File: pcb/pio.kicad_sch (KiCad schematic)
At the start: 32 parts, among them J11 BM04B-SRSS-TB, J4 BM06B-SRSS-TB, J5 BM06B-SRSS-TB, J6 BM04B-SRSS-TB, J7 BM06B-SRSS-TB, U4 MCP23017T-E/ML

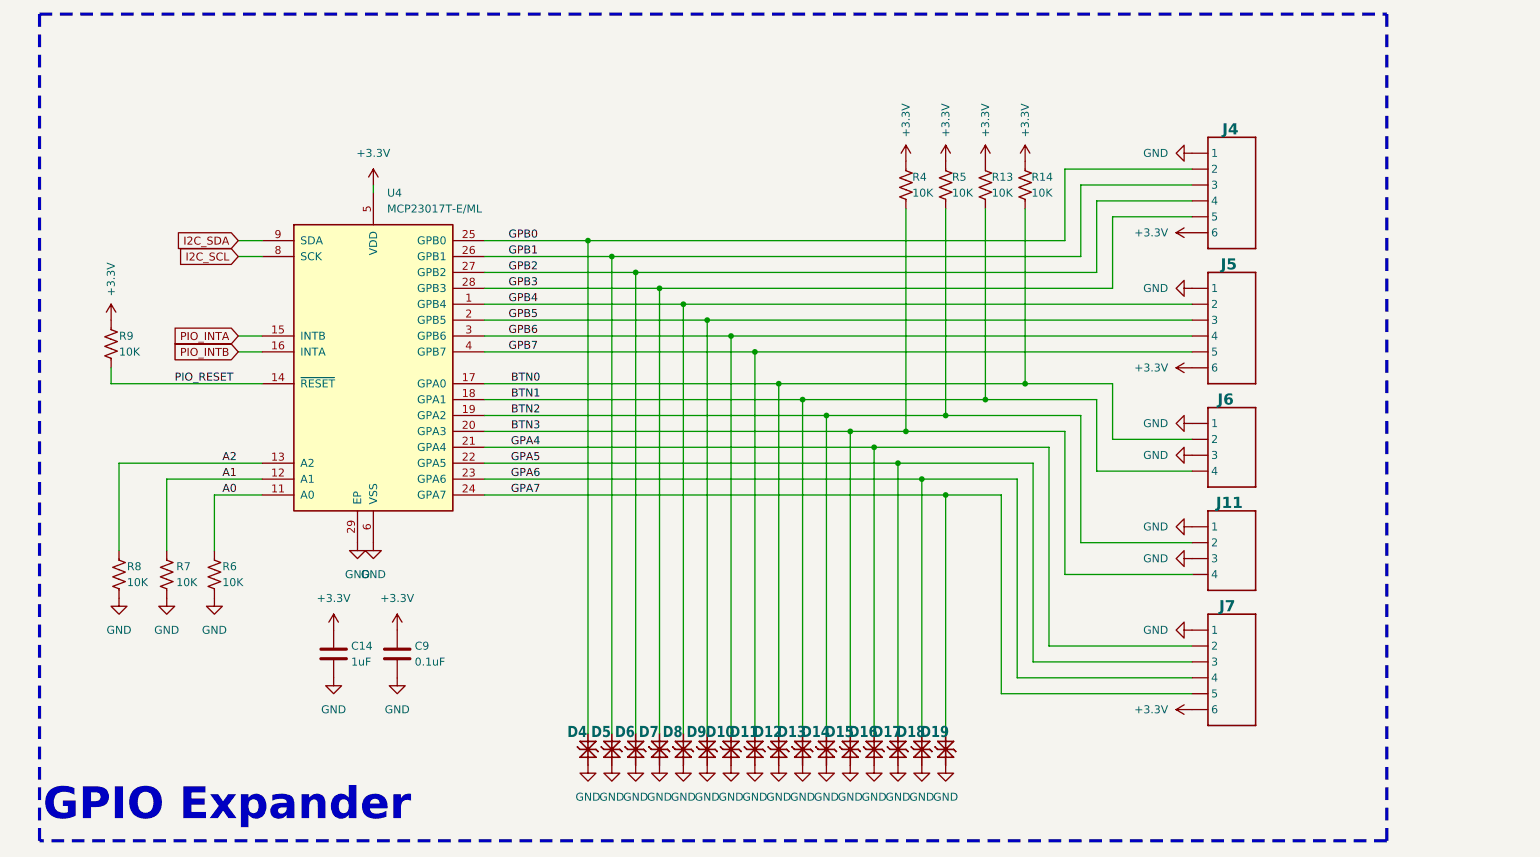
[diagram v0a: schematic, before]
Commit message: Updated license and minor schematic changes
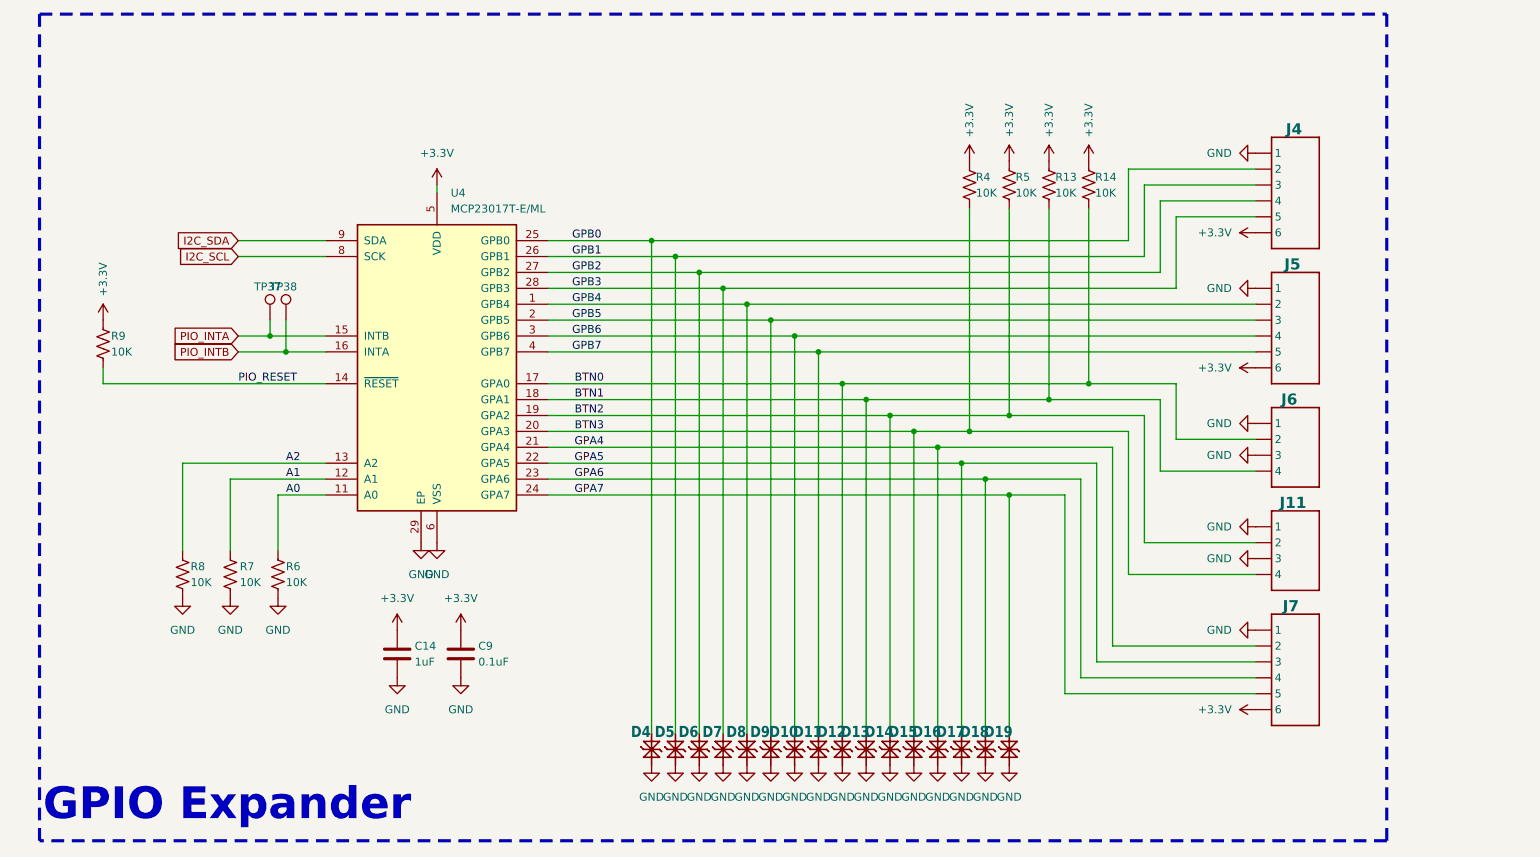
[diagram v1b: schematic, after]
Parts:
- added TP37, TP38: TP, CRGM Mechanical:TestPoint_Pad_D1.0mm, symbol Connector:TestPoint
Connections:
- net PIO_INTA: now also TP37.1
- net PIO_INTB: now also TP38.1
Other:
- moved on the sheet: C14, C9, D10, D11, D12, D13, D14, D15, D16, D17, D18, D19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

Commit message: Change name in schematic
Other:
- title: Node Hardware -> Hub Hardware
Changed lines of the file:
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@@
 	(paper "A4")
 	(title_block
-		(title "Node Hardware")
+		(title "Hub Hardware")
 		(date "<<release-date>>")
 		(rev "<<tag>>")

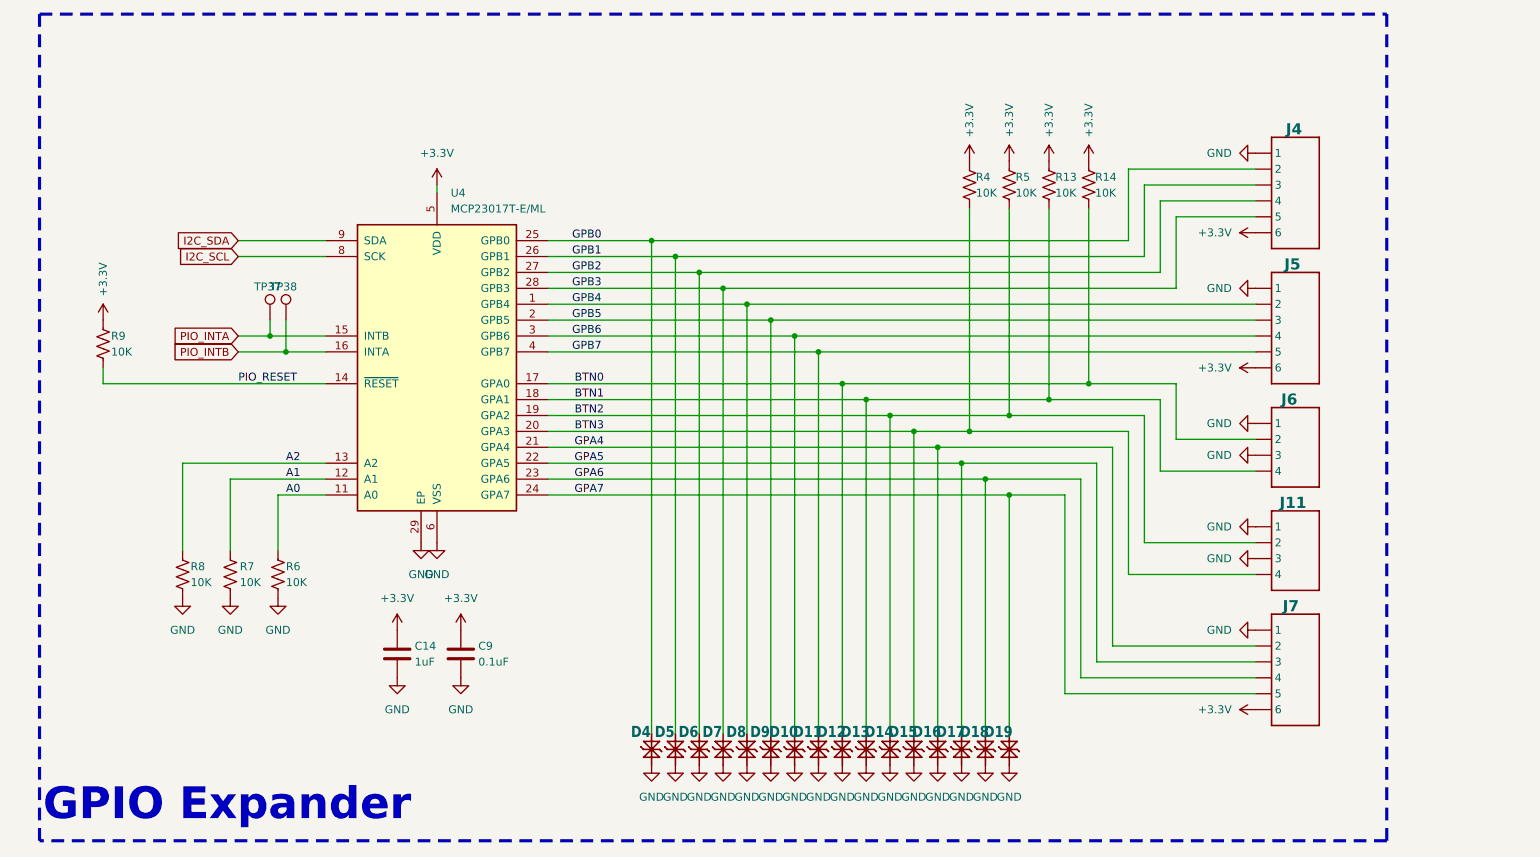
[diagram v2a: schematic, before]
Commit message: Renamed peripherals to interfaces; added test points; added led jumper
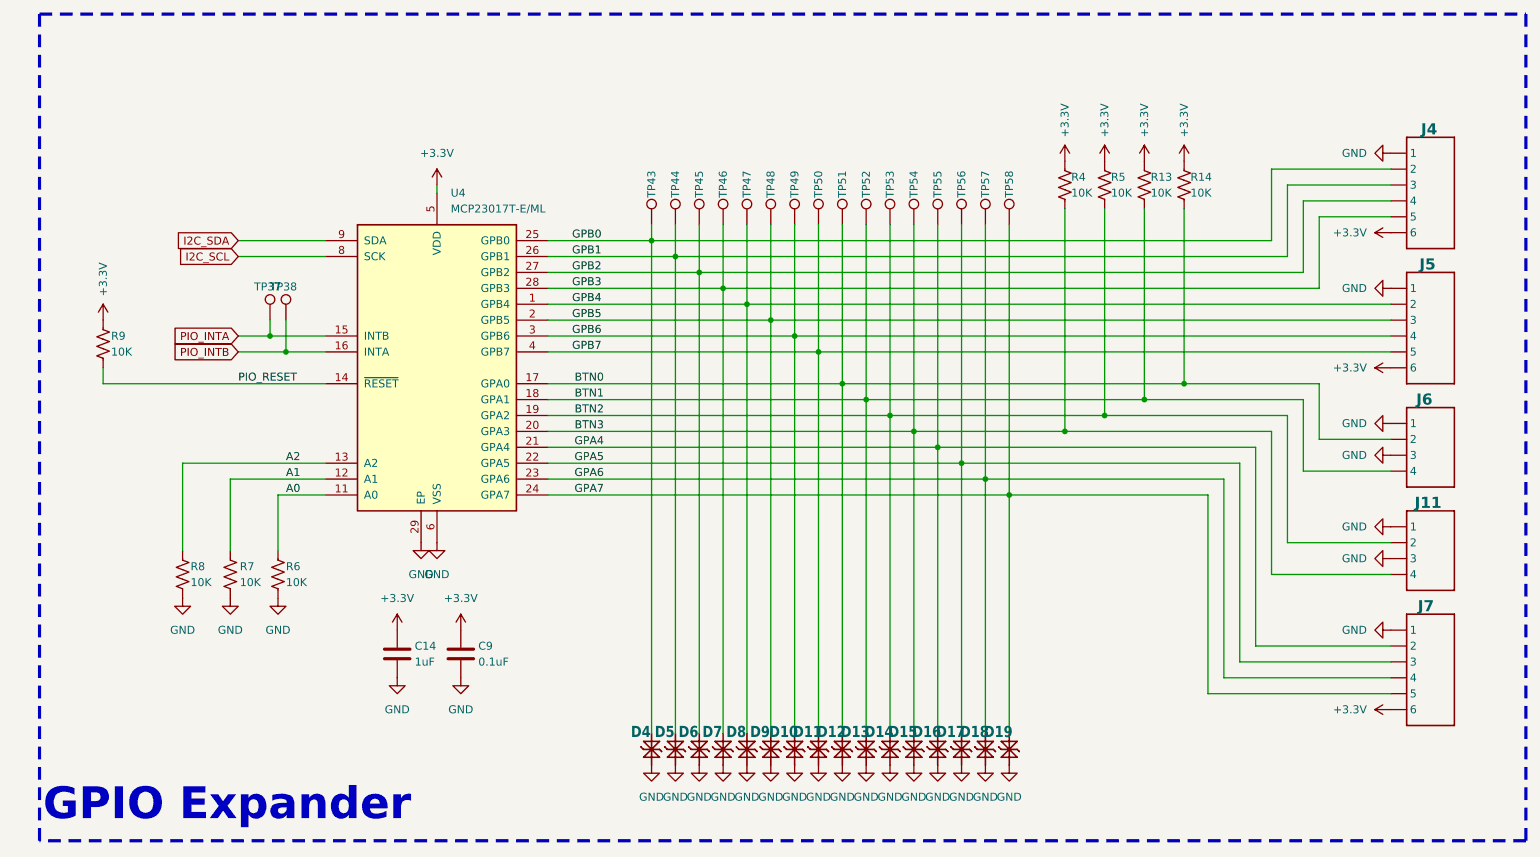
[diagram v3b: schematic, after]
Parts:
- added TP43, TP44, TP45, TP46, TP47, TP48, TP49, TP50, TP51, TP52, TP53, TP54, TP55, TP56, TP57, TP58: ~, CRGM Mechanical:TestPoint_Pad_D1.0mm, symbol Connector:TestPoint
- TP37, TP38: value TP -> ~
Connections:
- net BTN0: now also TP51.1
- net BTN1: now also TP52.1
- net BTN2: now also TP53.1
- net BTN3: now also TP54.1
- net GPA4: now also TP55.1
- net GPA5: now also TP56.1
- net GPA6: now also TP57.1
- net GPA7: now also TP58.1
- net GPB0: now also TP43.1
- net GPB1: now also TP44.1
- net GPB2: now also TP45.1
- net GPB3: now also TP46.1
- net GPB4: now also TP47.1
- net GPB5: now also TP48.1
- net GPB6: now also TP49.1
- net GPB7: now also TP50.1
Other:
- moved on the sheet: J11, J4, J5, J6, J7, R13, R14, R4, R5

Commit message: Adjusting for consistency
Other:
- title: Hub Hardware -> Aquarius Hub
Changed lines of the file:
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@@
 	(paper "A4")
 	(title_block
-		(title "Hub Hardware")
+		(title "Aquarius Hub")
 		(date "<<release-date>>")
 		(rev "<<tag>>")

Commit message: Sync symbols and footprints
Transitioned to CRGM footprints
Added dimensions
Fixed some spacing
Adjusted properties
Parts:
- C14, C9: footprint Capacitor_SMD:C_0603_1608Metric -> CRGM Passive:C_0603_1608Metric
- J11, J6: LCSC C2919601 -> C2763614
- J4, J5, J7: MPN BM06B-SRSS-TB -> BM06B-SRSS-TBT(LF)(SN)
- R13, R14, R4, R5, R6, R7, R8, R9: footprint Resistor_SMD:R_0603_1608Metric -> CRGM Passive:R_0603_1608Metric
- U4: footprint Package_DFN_QFN:QFN-28-1EP_6x6mm_P0.65mm_EP4.25x4.25mm -> CRG Makes:QFN-28-1EP_6x6mm_P0.65mm_EP4.25x4.25mm
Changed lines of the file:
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@@
 			)
 		)
-		(property "Footprint" "Resistor_SMD:R_0603_1608Metric"
+		(property "Footprint" "CRGM Passive:R_0603_1608Metric"
 			(at 200.406 43.434 90)
 			(effects
@@
 			)
 		)
-		(property "Footprint" "Resistor_SMD:R_0603_1608Metric"
+		(property "Footprint" "CRGM Passive:R_0603_1608Metric"
 			(at 48.006 105.664 90)
 			(effects
@@
 			)
 		)
-		(property "Footprint" "Package_DFN_QFN:QFN-28-1EP_6x6mm_P0.65mm_EP4.25x4.25mm"
+		(property "Footprint" "CRG Makes:QFN-28-1EP_6x6mm_P0.65mm_EP4.25x4.25mm"
 			(at 85.09 97.79 0)
 			(effects
@@
 			)
 		)
-		(property "Description" "JST SH 1.0mm 4 Position Vertical"
+		(property "Description" "4 Position, 1mm pitch"
 			(at 237.998 89.408 0)
 			(effects
@@
 			)
 		)
-		(property "LCSC" "C2919601"
+		(property "LCSC" "C2763614"
 			(at 237.998 80.01 0)
 			(effects
@@
 			)
 		)
-		(property "Footprint" "Capacitor_SMD:C_0603_1608Metric"
+		(property "Footprint" "CRGM Passive:C_0603_1608Metric"
 			(at 74.6252 121.92 0)
 			(effects
@@
 			)
 		)
-		(property "Footprint" "Resistor_SMD:R_0603_1608Metric"
+		(property "Footprint" "CRGM Passive:R_0603_1608Metric"
 			(at 187.706 43.434 90)
 			(effects
@@
 		)
 		(property "Footprint" "CRGM Connector:JST_SH_BM06B-SRSS-TB_1x06-1MP_P1.00mm_Vertical"
-			(at 234.95 114.3 0)
+			(at 236.474 104.648 0)
 			(effects
 				(font
@@
 			)
 		)
-		(property "Datasheet" "https://www.digikey.com/en/products/detail/jst-sales-america-inc/BM06B-SRSS-TB/926698"
-			(at 234.95 114.3 0)
+		(property "Datasheet" "https://www.jst-mfg.com/product/pdf/eng/eSH.pdf"
+			(at 235.712 141.478 0)
 			(effects
 				(font
@@
 			)
 		)
-		(property "Description" "JST SH 1.0mm 6 Position Vertical"
-			(at 234.95 114.3 0)
+		(property "Description" "6 position, 1mm pitch"
+			(at 236.982 106.68 0)
 			(effects
 				(font
@@
 		)
 		(property "LCSC" "C2845374"
-			(at 234.95 114.3 0)
+			(at 235.458 139.7 0)
 			(effects
 				(font
@@
 		)
 		(property "MN" "JST"
-			(at 234.95 114.3 0)
+			(at 234.95 132.842 0)
 			(effects
 				(font
@@
 			)
 		)
-		(property "MPN" "BM06B-SRSS-TB"
-			(at 234.95 114.3 0)
+		(property "MPN" "BM06B-SRSS-TBT(LF)(SN)"
+			(at 234.95 134.366 0)
 			(effects
 				(font
@@
 		)
 		(property "Digikey" "455-BM06B-SRSS-TBTR-ND"
-			(at 234.95 114.3 0)
+			(at 234.95 137.922 0)
 			(effects
 				(font
@@
 		)
 		(property "Mouser" "306-BM06BSRSSTBTLFSN"
-			(at 234.95 114.3 0)
+			(at 234.696 136.144 0)
 			(effects
 				(font
@@
 			)
 		)
-		(property "Footprint" "Resistor_SMD:R_0603_1608Metric"
+		(property "Footprint" "CRGM Passive:R_0603_1608Metric"
 			(at 181.356 43.434 90)
 			(effects
@@
 			)
 		)
-		(property "Footprint" "Resistor_SMD:R_0603_1608Metric"
+		(property "Footprint" "CRGM Passive:R_0603_1608Metric"
 			(at 40.386 105.664 90)
 			(effects
@@
 		)
 		(property "Footprint" "CRGM Connector:JST_SH_BM06B-SRSS-TB_1x06-1MP_P1.00mm_Vertical"
-			(at 234.95 38.1 0)
+			(at 236.474 28.448 0)
 			(effects
 				(font
@@
 			)
 		)
-		(property "Datasheet" "https://www.digikey.com/en/products/detail/jst-sales-america-inc/BM06B-SRSS-TB/926698"
-			(at 234.95 38.1 0)
+		(property "Datasheet" "https://www.jst-mfg.com/product/pdf/eng/eSH.pdf"
+			(at 235.712 65.278 0)
 			(effects
 				(font
@@
 			)
 		)
-		(property "Description" "JST SH 1.0mm 6 Position Vertical"
-			(at 234.95 38.1 0)
+		(property "Description" "6 position, 1mm pitch"
+			(at 236.982 30.48 0)
 			(effects
 				(font
@@
 		)
 		(property "LCSC" "C2845374"
-			(at 234.95 38.1 0)
+			(at 235.458 63.5 0)
 			(effects
 				(font
@@
 		)
 		(property "MN" "JST"
-			(at 234.95 38.1 0)
+			(at 234.95 56.642 0)
 			(effects
 				(font
@@
 			)
 		)
-		(property "MPN" "BM06B-SRSS-TB"
-			(at 234.95 38.1 0)
+		(property "MPN" "BM06B-SRSS-TBT(LF)(SN)"
+			(at 234.95 58.166 0)
 			(effects
 				(font
@@
 		)
 		(property "Digikey" "455-BM06B-SRSS-TBTR-ND"
-			(at 234.95 38.1 0)
+			(at 234.95 61.722 0)
 			(effects
 				(font
@@
 		)
 		(property "Mouser" "306-BM06BSRSSTBTLFSN"
-			(at 234.95 38.1 0)
+			(at 234.696 59.944 0)
 			(effects
 				(font
@@
 			)
 		)
-		(property "Footprint" "Resistor_SMD:R_0603_1608Metric"
+		(property "Footprint" "CRGM Passive:R_0603_1608Metric"
 			(at 194.056 43.434 90)
 			(effects
@@
 	)
 	(symbol
-		(lib_name "JST-SH-4_1")
 		(lib_id "CRGM Connector:JST-SH-4")
 		(at 234.95 88.9 0)
@@
 			)
 		)
-		(property "Description" "JST SH 1.0mm 4 Position Vertical"
+		(property "Description" "4 Position, 1mm pitch"
 			(at 237.998 72.898 0)
 			(effects
@@
 			)
 		)
-		(property "LCSC" "C2919601"
+		(property "LCSC" "C2763614"
 			(at 237.998 63.5 0)
 			(effects
@@
 		)
 		(property "Footprint" "CRGM Connector:JST_SH_BM06B-SRSS-TB_1x06-1MP_P1.00mm_Vertical"
-			(at 234.95 59.69 0)
+			(at 236.474 50.038 0)
 			(effects
 				(font
@@
 			)
 		)
-		(property "Datasheet" "https://www.digikey.com/en/products/detail/jst-sales-america-inc/BM06B-SRSS-TB/926698"
-			(at 234.95 59.69 0)
+		(property "Datasheet" "https://www.jst-mfg.com/product/pdf/eng/eSH.pdf"
+			(at 235.712 86.868 0)
 			(effects
 				(font
@@
 			)
 		)
-		(property "Description" "JST SH 1.0mm 6 Position Vertical"
-			(at 234.95 59.69 0)
+		(property "Description" "6 position, 1mm pitch"
+			(at 236.982 52.07 0)
 			(effects
 				(font
@@
 		)
 		(property "LCSC" "C2845374"
-			(at 234.95 59.69 0)
+			(at 235.458 85.09 0)
 			(effects
 				(font
@@
 		)
 		(property "MN" "JST"
-			(at 234.95 59.69 0)
+			(at 234.95 78.232 0)
 			(effects
 				(font
@@
 			)
 		)
-		(property "MPN" "BM06B-SRSS-TB"
-			(at 234.95 59.69 0)
+		(property "MPN" "BM06B-SRSS-TBT(LF)(SN)"
+			(at 234.95 79.756 0)
 			(effects
 				(font
@@
 		)
 		(property "Digikey" "455-BM06B-SRSS-TBTR-ND"
-			(at 234.95 59.69 0)
+			(at 234.95 83.312 0)
 			(effects
 				(font
@@
 		)
 		(property "Mouser" "306-BM06BSRSSTBTLFSN"
-			(at 234.95 59.69 0)
+			(at 234.696 81.534 0)
 			(effects
 				(font
@@
 			)
 		)
-		(property "Footprint" "Resistor_SMD:R_0603_1608Metric"
+		(property "Footprint" "CRGM Passive:R_0603_1608Metric"
 			(at 27.686 68.834 90)
 			(effects
@@
 			)
 		)
-		(property "Footprint" "Capacitor_SMD:C_0603_1608Metric"
+		(property "Footprint" "CRGM Passive:C_0603_1608Metric"
 			(at 84.7852 121.92 0)
 			(effects
@@
 			)
 		)
-		(property "Footprint" "Resistor_SMD:R_0603_1608Metric"
+		(property "Footprint" "CRGM Passive:R_0603_1608Metric"
 			(at 55.626 105.664 90)
 			(effects

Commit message: Clean up and consistency
Moved buzzer to MCU
Fixed model directory
Set font size
Set outline size
Upscaled Roxy ❤️
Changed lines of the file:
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@@
 	)
 	(rectangle
-		(start 16.51 15.875)
-		(end 254 147.955)
+		(start 15.24 15.875)
+		(end 254 147.32)
 		(stroke
-			(width 0.508)
+			(width 0.254)
 			(type dash)
 			(color 255 153 0 1)
@@
 	(text "GPIO Expander"
 		(exclude_from_sim yes)
-		(at 46.482 142.24 0)
+		(at 15.24 147.32 0)
 		(effects
 			(font
 				(face "KiCad Font")
-				(size 5.08 5.08)
+				(size 3 3)
 				(thickness 1.016)
 				(bold yes)
-				(color 255 153 0 1)
+				(color 0 0 194 1)
 			)
+			(justify left bottom)
 		)
 	)

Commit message: Updated part attributes for consistency.
Updated requirements section to be more accurate.
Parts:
- C14, C9: Tolerance (none) -> 10%
- R13, R14, R4, R5, R6, R7, R8, R9: Tolerance (none) -> 5%
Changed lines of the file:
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@@
 			)
 		)
+		(property "Tolerance" "5%"
+			(at 199.39 43.18 0)
+			(effects
+				(font
+					(size 1.27 1.27)
+				)
+				(hide yes)
+			)
+		)
 		(pin "2"
 		)
@@
 			)
 		)
+		(property "Tolerance" "5%"
+			(at 46.99 105.41 0)
+			(effects
+				(font
+					(size 1.27 1.27)
+				)
+				(hide yes)
+			)
+		)
 		(pin "2"
 		)
@@
 			)
 		)
+		(property "Tolerance" "10%"
+			(at 73.66 118.11 0)
+			(effects
+				(font
+					(size 1.27 1.27)
+				)
+				(hide yes)
+			)
+		)
 		(pin "1"
 		)
@@
 			)
 		)
+		(property "Tolerance" "5%"
+			(at 186.69 43.18 0)
+			(effects
+				(font
+					(size 1.27 1.27)
+				)
+				(hide yes)
+			)
+		)
 		(pin "2"
 		)
@@
 			)
 		)
+		(property "Tolerance" "5%"
+			(at 180.34 43.18 0)
+			(effects
+				(font
+					(size 1.27 1.27)
+				)
+				(hide yes)
+			)
+		)
 		(pin "2"
 		)
@@
 			)
 		)
+		(property "Tolerance" "5%"
+			(at 39.37 105.41 0)
+			(effects
+				(font
+					(size 1.27 1.27)
+				)
+				(hide yes)
+			)
+		)
 		(pin "2"
 		)
@@
 			)
 		)
+		(property "Tolerance" "5%"
+			(at 193.04 43.18 0)
+			(effects
+				(font
+					(size 1.27 1.27)
+				)
+				(hide yes)
+			)
+		)
 		(pin "2"
 		)
@@
 			)
 		)
+		(property "Tolerance" "5%"
+			(at 26.67 68.58 0)
+			(effects
+				(font
+					(size 1.27 1.27)
+				)
+				(hide yes)
+			)
+		)
 		(pin "2"
 		)
@@
 			)
 		)
+		(property "Tolerance" "10%"
+			(at 83.82 118.11 0)
+			(effects
+				(font
+					(size 1.27 1.27)
+				)
+				(hide yes)
+			)
+		)
 		(pin "1"
 		)
@@
 			(at 54.61 105.41 0)
 			(effects
+				(font
+					(size 1.27 1.27)
+				)
+				(hide yes)
+			)
+		)
+		(property "Tolerance" "5%"
+			(at 54.61 105.41 0)
+			(effects

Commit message: fixed LCSC part numbers
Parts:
- J11, J6: LCSC C2763614 -> C2904986
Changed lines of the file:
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@@
 			)
 		)
-		(property "LCSC" "C2763614"
+		(property "LCSC" "C2904986"
 			(at 237.998 80.01 0)
 			(effects
@@
 			)
 		)
-		(property "LCSC" "C2763614"
+		(property "LCSC" "C2904986"
 			(at 237.998 63.5 0)
 			(effects
